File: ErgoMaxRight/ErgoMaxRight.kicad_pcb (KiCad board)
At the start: 2 copper layers, 182.8 x 169.2 mm, 98 parts, among them J1 PJ-320A, K1 KEYSW, K10 KEYSW, K11 KEYSW, K12 KEYSW, K13 KEYSW, K14 KEYSW, K15 KEYSW, K16 KEYSW, K17 KEYSW, K18 KEYSW, K19 KEYSW, K2 KEYSW, K20 KEYSW, K21 KEYSW, K22 KEYSW, K23 KEYSW, K24 KEYSW, K25 KEYSW, K26 KEYSW, K27 KEYSW, K28 KEYSW, K29 KEYSW, K3 KEYSW, K30 KEYSW, K31 KEYSW, K32 KEYSW, K33 KEYSW, K34 KEYSW, K35 KEYSW, K36 KEYSW, K37 KEYSW, K38 KEYSW, K39 KEYSW, K4 KEYSW, K40 KEYSW, K41 KEYSW, K42 KEYSW, K43 KEYSW, K44 KEYSW, K5 KEYSW, K6 KEYSW, K7 KEYSW, K8 KEYSW, K9 KEYSW, U1 ProMicro

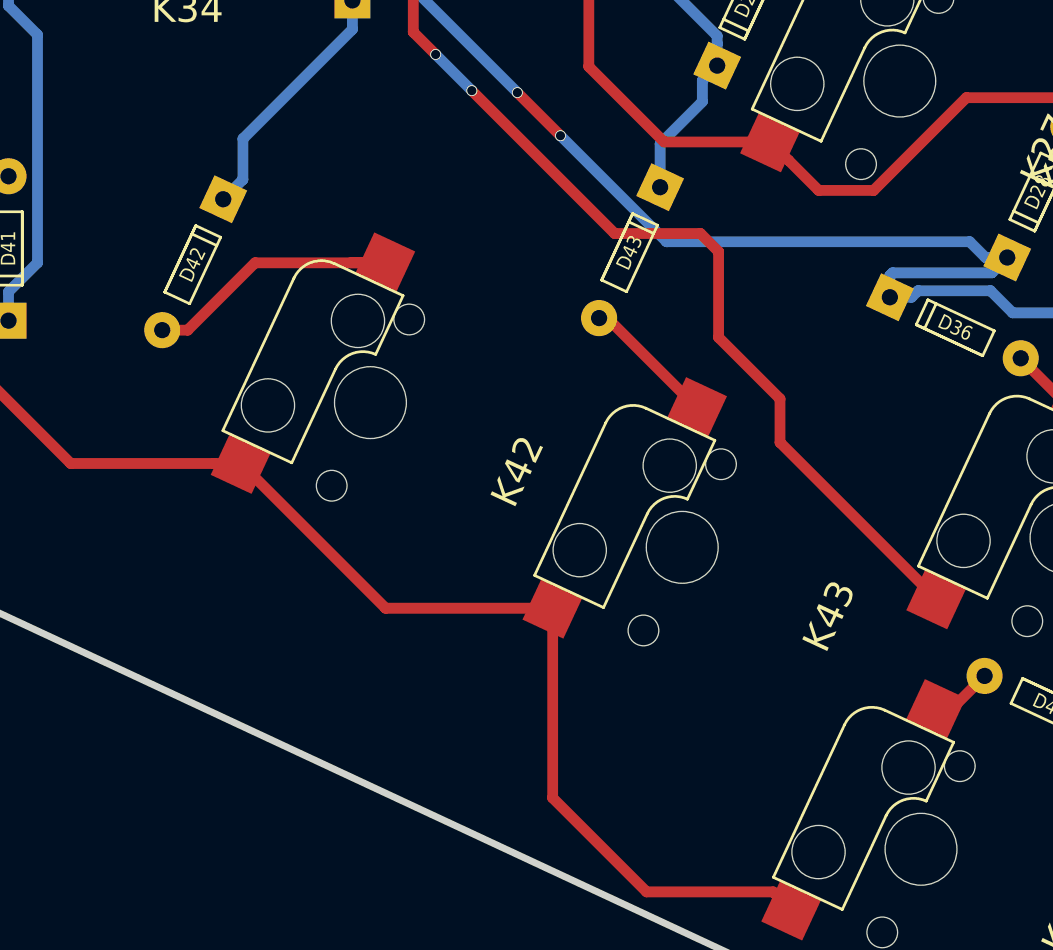
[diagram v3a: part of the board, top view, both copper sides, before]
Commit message: add missing stabs in schema, add them back in PCB
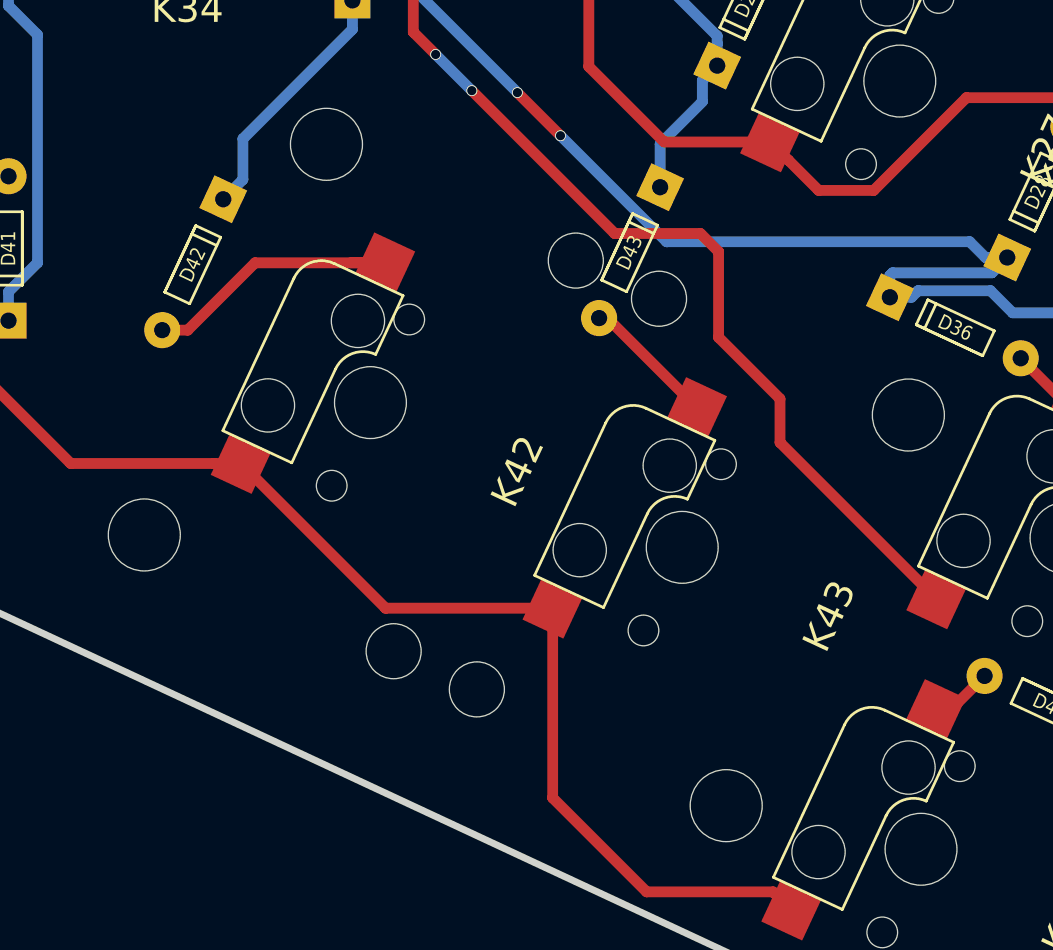
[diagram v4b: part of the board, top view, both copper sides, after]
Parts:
- added St1: Stab 2U, keyboard_parts:Mx_Stab_200, F.Cu at (252.2, 176.7)
- added St2: Stab 2U, keyboard_parts:Mx_Stab_200, F.Cu at (235.0, 168.7)
